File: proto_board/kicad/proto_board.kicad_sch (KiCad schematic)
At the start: 7 parts, among them J1 pcie_98, J2 Conn_02x25_Odd_Even, J3 Conn_02x25_Odd_Even

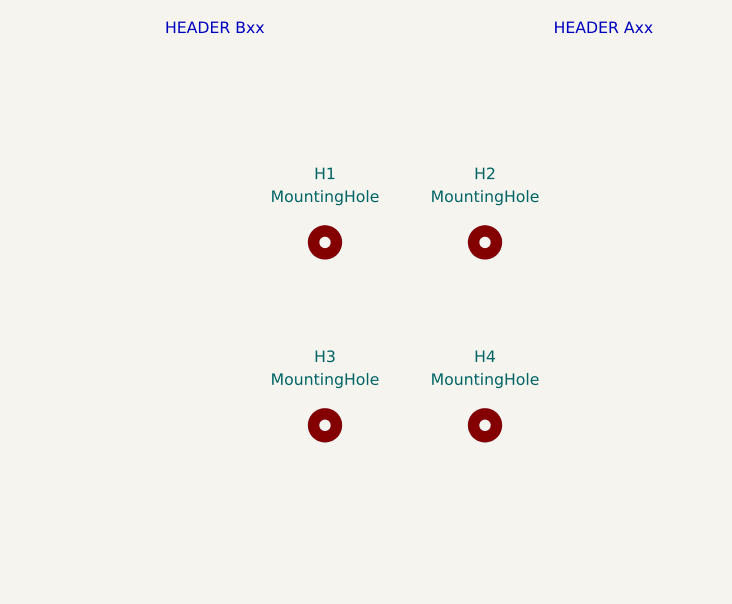
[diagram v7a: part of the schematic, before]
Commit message: Updated proto board to the common card outline.
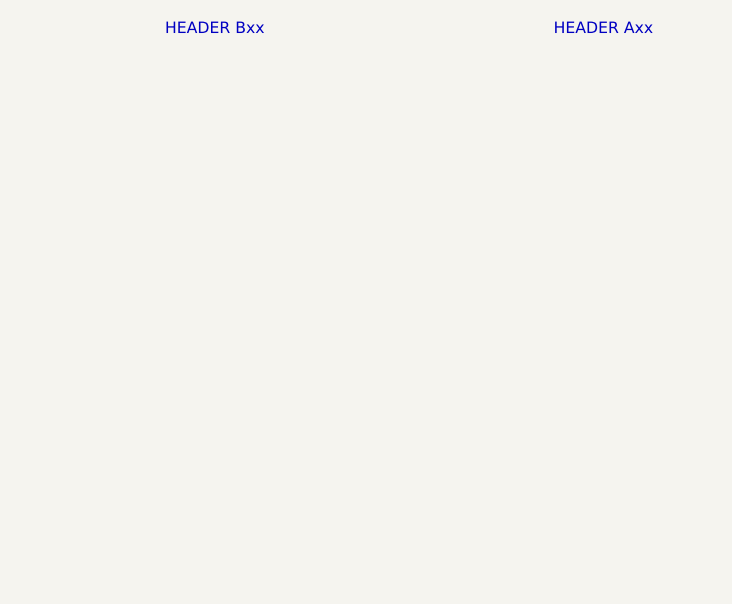
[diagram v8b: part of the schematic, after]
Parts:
- removed H1, H2, H3, H4: MountingHole, MountingHole:MountingHole_3.2mm_M3_Pad_Via, symbol Mechanical:MountingHole
- J1: footprint proto_board:pcie_98_edge -> common:PCIE_98_CARD
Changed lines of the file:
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@@
     (effects (font (size 1.27 1.27)) (justify right bottom))
-  )
-  (symbol (lib_id "Mechanical:MountingHole") (at 172.72 157.48 0) (unit 1)
-    (in_bom yes) (on_board yes) (dnp no)
-    (property "Reference" "H4" (at 172.72 149.86 0)
-      (effects (font (size 1.27 1.27)))
-    )
-    (property "Value" "MountingHole" (at 172.72 152.4 0)
-      (effects (font (size 1.27 1.27)))
-    )
-    (property "Footprint" "MountingHole:MountingHole_3.2mm_M3_Pad_Via" (at 172.72 157.48 0)
-      (effects (font (size 1.27 1.27)) hide)
-    )
-    (property "Datasheet" "~" (at 172.72 157.48 0)
-      (effects (font (size 1.27 1.27)) hide)
-    )
-    (instances
-      (project "proto_board"
-        (path "/0dcd9c8c-bd5a-437f-856e-101fb6cf8b66"
-          (reference "H4") (unit 1)
-        )
-      )
-    )
-  )
-  (symbol (lib_id "Mechanical:MountingHole") (at 154.94 157.48 0) (unit 1)
-    (in_bom yes) (on_board yes) (dnp no)
-    (property "Reference" "H3" (at 154.94 149.86 0)
-      (effects (font (size 1.27 1.27)))
-    )
-    (property "Value" "MountingHole" (at 154.94 152.4 0)
-      (effects (font (size 1.27 1.27)))
-    )
-    (property "Footprint" "MountingHole:MountingHole_3.2mm_M3_Pad_Via" (at 154.94 157.48 0)
-      (effects (font (size 1.27 1.27)) hide)
-    )
-    (property "Datasheet" "~" (at 154.94 157.48 0)
-      (effects (font (size 1.27 1.27)) hide)
-    )
-    (instances
-      (project "proto_board"
-        (path "/0dcd9c8c-bd5a-437f-856e-101fb6cf8b66"
-          (reference "H3") (unit 1)
-        )
-      )
-    )
-  )
-  (symbol (lib_id "Mechanical:MountingHole") (at 172.72 137.16 0) (unit 1)
-    (in_bom yes) (on_board yes) (dnp no)
-    (property "Reference" "H2" (at 172.72 129.54 0)
-      (effects (font (size 1.27 1.27)))
-    )
-    (property "Value" "MountingHole" (at 172.72 132.08 0)
-      (effects (font (size 1.27 1.27)))
-    )
-    (property "Footprint" "MountingHole:MountingHole_3.2mm_M3_Pad_Via" (at 172.72 137.16 0)
-      (effects (font (size 1.27 1.27)) hide)
-    )
-    (property "Datasheet" "~" (at 172.72 137.16 0)
-      (effects (font (size 1.27 1.27)) hide)
-    )
-    (instances
-      (project "proto_board"
-        (path "/0dcd9c8c-bd5a-437f-856e-101fb6cf8b66"
-          (reference "H2") (unit 1)
-        )
-      )
-    )
   )
   (symbol (lib_id "proto_board:pcie_98") (at 73.66 81.28 0) (unit 1)
@@
       (effects (font (size 1.27 1.27)))
     )
-    (property "Footprint" "proto_board:pcie_98_edge" (at 99.949 32.766 0)
+    (property "Footprint" "common:PCIE_98_CARD" (at 99.949 32.766 0)
       (effects (font (size 1.27 1.27)) hide)
     )
@@
         )
       )
-    )
-  )
-  (symbol (lib_id "Mechanical:MountingHole") (at 154.94 137.16 0) (unit 1)
-    (in_bom yes) (on_board yes) (dnp no)
-    (property "Reference" "H1" (at 154.94 129.54 0)
-      (effects (font (size 1.27 1.27)))
-    )
-    (property "Value" "MountingHole" (at 154.94 132.08 0)
-      (effects (font (size 1.27 1.27)))
-    )
-    (property "Footprint" "MountingHole:MountingHole_3.2mm_M3_Pad_Via" (at 154.94 137.16 0)
-      (effects (font (size 1.27 1.27)) hide)
-    )
-    (property "Datasheet" "~" (at 154.94 137.16 0)
-      (effects (font (size 1.27 1.27)) hide)
-    )
-    (instances
-      (project "proto_board"
-        (path "/0dcd9c8c-bd5a-437f-856e-101fb6cf8b66"
-          (reference "H1") (unit 1)
-        )
-      )
